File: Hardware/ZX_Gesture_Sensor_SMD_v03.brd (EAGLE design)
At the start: 57.2 x 19.1 mm, 51 parts, among them Q1 MMBT2222A, Q2 MOSFET-NCHANNEL2N7002PW, U1 PIC16F1823-14PINTSSOP, U2 MCP6021T-E/OT, U3 DMC2700UDM, U4 DMC2700UDM, U6 TSOP57238TT1

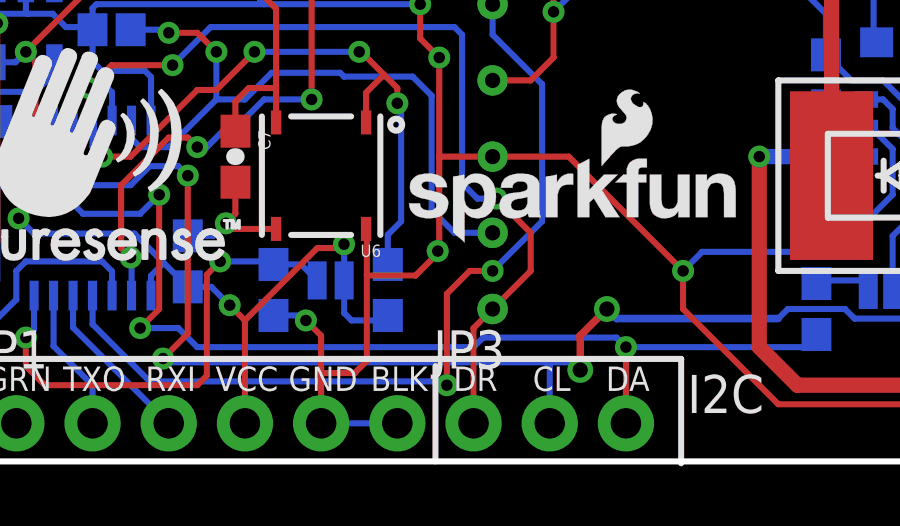
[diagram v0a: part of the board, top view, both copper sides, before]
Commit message: Updated Brd and Sch Files per QC review
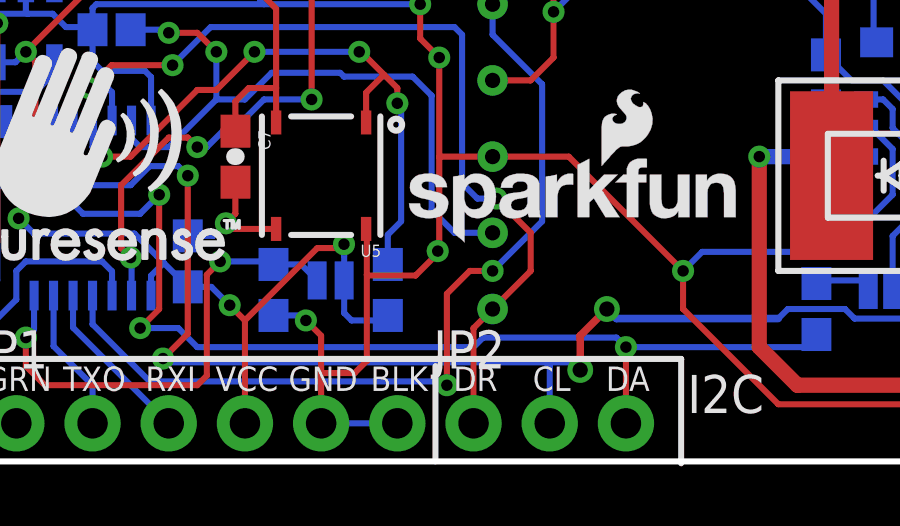
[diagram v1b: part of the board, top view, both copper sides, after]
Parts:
- moved TP3 5.08 mm to (34.3, 10.2)
- moved TP1 2.54 mm to (34.3, 15.2), turned to 0 degrees
- moved TP4 2.54 mm to (34.3, 7.62)
- moved TP5 2.54 mm to (34.3, 5.08)
- moved TP2 2.54 mm to (34.3, 12.7), turned to 90 degrees
- renumbered JP3 to JP2, U6 to U5
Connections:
- net GND: now also TP3.P$1; no longer TP2.P$1
- net ICSPCLK/DATA_RDY: now also TP5.P$1; no longer TP4.P$1
- net ICSPDAT/DACOUT: now also TP4.P$1; no longer TP5.P$1
- net MCLR: now also TP1.P$1; no longer TP3.P$1
- net VCC: now also TP2.P$1; no longer TP1.P$1
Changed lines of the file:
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@@
 <attribute name="PROD_ID" value="TRANS-11993" x="80.9625" y="-15.5575" size="1.778" layer="28" rot="MR270" display="off"/>
 </element>
-<element name="U6" library="SparkFun-Sensors" package="TSOP572" value="TSOP57238TT1" x="28.575" y="9.525" rot="R180">
+<element name="U5" library="SparkFun-Sensors" package="TSOP572" value="TSOP57238TT1" x="28.575" y="9.525" rot="R180">
 <attribute name="PROD_ID" value="COMP-11990" x="13.335" y="42.545" size="1.778" layer="27" rot="R180" display="off"/>
 </element>
@@
 <attribute name="PROD_ID" value="CONN-08437" x="18.415" y="1.27" size="1.778" layer="27" display="off"/>
 </element>
-<element name="JP3" library="SparkFun-Connectors" package="1X03_NO_SILK" value="" x="33.655" y="1.27"/>
+<element name="JP2" library="SparkFun-Connectors" package="1X03_NO_SILK" value="" x="33.655" y="1.27"/>
 <element name="R1" library="SparkFun-Resistors" package="0603-RES" value="100k" x="22.225" y="15.24" rot="MR90">
 <attribute name="PROD_ID" value="RES-07828" x="-26.035" y="30.48" size="1.778" layer="28" rot="MR90" display="off"/>
@@
 </element>
 <element name="R3" library="SparkFun-Resistors" package="0603-RES" value="10" x="15.24" y="10.16" rot="MR90">
-<attribute name="PROD_ID" value="RES-12581" x="-33.02" y="33.02" size="1.778" layer="28" rot="MR90" display="off"/>
-<attribute name="TOL" value="1%" x="15.24" y="10.16" size="1.778" layer="28" rot="MR90" display="off"/>
+<attribute name="PROD_ID" value="RES-09834" x="-33.02" y="33.02" size="1.778" layer="28" rot="MR90" display="off"/>
 </element>
 <element name="R4" library="SparkFun-Resistors" package="0603-RES" value="1K" x="17.78" y="10.4775" rot="MR270">
@@
 <element name="STANDOFF1" library="SparkFun-Electromechanical" package="STAND-OFF" value="STAND-OFF" x="2.54" y="9.525"/>
 <element name="STANDOFF2" library="SparkFun-Electromechanical" package="STAND-OFF" value="STAND-OFF" x="54.61" y="9.525" rot="R90"/>
-<element name="TP1" library="SparkFun-Passives" package="PAD.03X.04" value="TEST-POINT3X4" x="34.29" y="12.7" rot="MR90"/>
-<element name="TP2" library="SparkFun-Passives" package="PAD.03X.04" value="TEST-POINT3X4" x="34.29" y="10.16" rot="MR0"/>
-<element name="TP3" library="SparkFun-Passives" package="PAD.03X.04" value="TEST-POINT3X4" x="34.29" y="15.24" rot="MR0"/>
-<element name="TP4" library="SparkFun-Passives" package="PAD.03X.04" value="TEST-POINT3X4" x="34.29" y="5.08" rot="MR0"/>
-<element name="TP5" library="SparkFun-Passives" package="PAD.03X.04" value="TEST-POINT3X4" x="34.29" y="7.62" rot="MR0"/>
+<element name="TP2" library="SparkFun-Passives" package="PAD.03X.04" value="TEST-POINT3X4" x="34.29" y="12.7" rot="MR90"/>
+<element name="TP3" library="SparkFun-Passives" package="PAD.03X.04" value="TEST-POINT3X4" x="34.29" y="10.16" rot="MR0"/>
+<element name="TP1" library="SparkFun-Passives" package="PAD.03X.04" value="TEST-POINT3X4" x="34.29" y="15.24" rot="MR0"/>
+<element name="TP5" library="SparkFun-Passives" package="PAD.03X.04" value="TEST-POINT3X4" x="34.29" y="5.08" rot="MR0"/>
+<element name="TP4" library="SparkFun-Passives" package="PAD.03X.04" value="TEST-POINT3X4" x="34.29" y="7.62" rot="MR0"/>
 <element name="U$6" library="SparkFun-Aesthetics" package="GESTURESENSE_TEXT" value="GESTURESENSE_LOGOSTEXT" x="14.351" y="6.223"/>
 <element name="D1" library="SparkFun-LED" package="SFH4641-SHORT2" value="SFH4641SHORT2" x="9.525" y="9.525" rot="R270">
@@
 <contactref element="C5" pad="1"/>
 <contactref element="U4" pad="S2"/>
-<contactref element="U6" pad="5"/>
+<contactref element="U5" pad="5"/>
 <contactref element="C7" pad="1"/>
 <contactref element="R9" pad="2"/>
@@
 <contactref element="SJ1" pad="2"/>
 <contactref element="SJ2" pad="2"/>
-<contactref element="TP1" pad="P$1"/>
+<contactref element="TP2" pad="P$1"/>
 <contactref element="C4" pad="2"/>
 <contactref element="C6" pad="2"/>
@@
 <contactref element="C5" pad="2"/>
 <contactref element="C7" pad="2"/>
-<contactref element="U6" pad="6"/>
-<contactref element="U6" pad="8"/>
+<contactref element="U5" pad="6"/>
+<contactref element="U5" pad="8"/>
 <contactref element="U1" pad="14"/>
 <contactref element="C8" pad="2"/>
 <contactref element="R12" pad="1"/>
-<contactref element="TP2" pad="P$1"/>
+<contactref element="TP3" pad="P$1"/>
 <via x="34.29" y="10.16" extent="1-16" drill="0.508" diameter="1.016"/>
 <polygon width="0.2032" layer="16" isolate="0.3048">
@@
 </signal>
 <signal name="I2C_SDA">
-<contactref element="JP3" pad="3"/>
+<contactref element="JP2" pad="3"/>
 <contactref element="R10" pad="1"/>
 <contactref element="U1" pad="9"/>
@@
 </signal>
 <signal name="I2C_SCL">
-<contactref element="JP3" pad="2"/>
+<contactref element="JP2" pad="2"/>
 <contactref element="R11" pad="1"/>
 <contactref element="U1" pad="10"/>
@@
 <signal name="ICSPDAT/DACOUT">
 <contactref element="U1" pad="13"/>
-<contactref element="TP5" pad="P$1"/>
+<contactref element="TP4" pad="P$1"/>
 <contactref element="R1" pad="1"/>
 <via x="23.495" y="14.2875" extent="1-16" drill="0.381"/>
@@
 <signal name="ICSPCLK/DATA_RDY">
 <contactref element="U1" pad="12"/>
-<contactref element="JP3" pad="1"/>
-<contactref element="TP4" pad="P$1"/>
+<contactref element="JP2" pad="1"/>
+<contactref element="TP5" pad="P$1"/>
 <via x="34.29" y="5.08" extent="1-16" drill="0.508" diameter="1.016"/>
 <wire x1="21.59" y1="13.208" x2="20.828" y2="12.446" width="0.2032" layer="1"/>
@@
 <signal name="MCLR">
 <contactref element="U1" pad="4"/>
-<contactref element="TP3" pad="P$1"/>
+<contactref element="TP1" pad="P$1"/>
 <via x="34.29" y="15.24" extent="1-16" drill="0.508" diameter="1.016"/>
 <via x="32.766" y="2.54" extent="1-16" drill="0.381"/>
@@
 </signal>
 <signal name="RECEIVER">
-<contactref element="U6" pad="1"/>
+<contactref element="U5" pad="1"/>
 <contactref element="U1" pad="11"/>
 <contactref element="R9" pad="1"/>
